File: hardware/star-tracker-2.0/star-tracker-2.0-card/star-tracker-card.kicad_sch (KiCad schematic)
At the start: 8 parts, among them J1 TFM-120-01-L-D-RA, J2 SM14B-SHLS-TF, J3 GRPB041VWVN-RC, J4 3-2492104-6

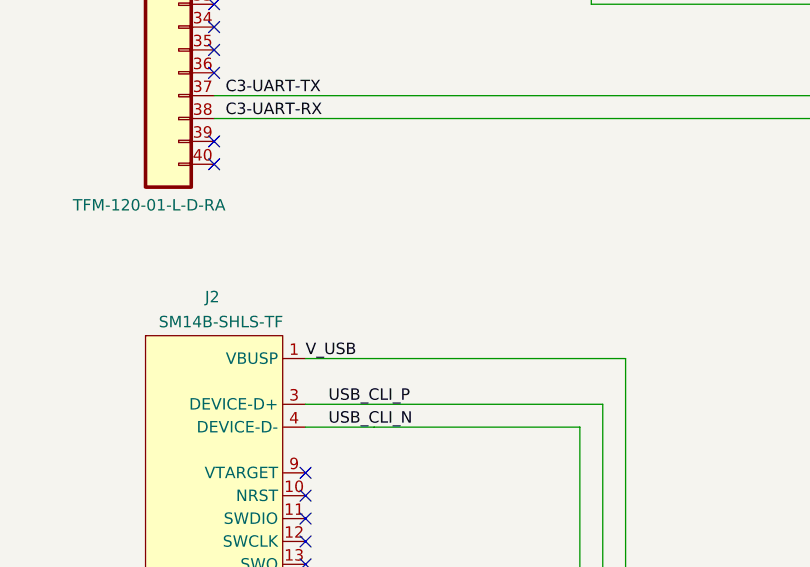
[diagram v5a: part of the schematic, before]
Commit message: Finishing touches
added gitignore for .ds_store (mac file for kicad) changed bom details for components. added 3d models to footprints. Went over schematic checklist. Camera and star tracker ready for final DR for send off.
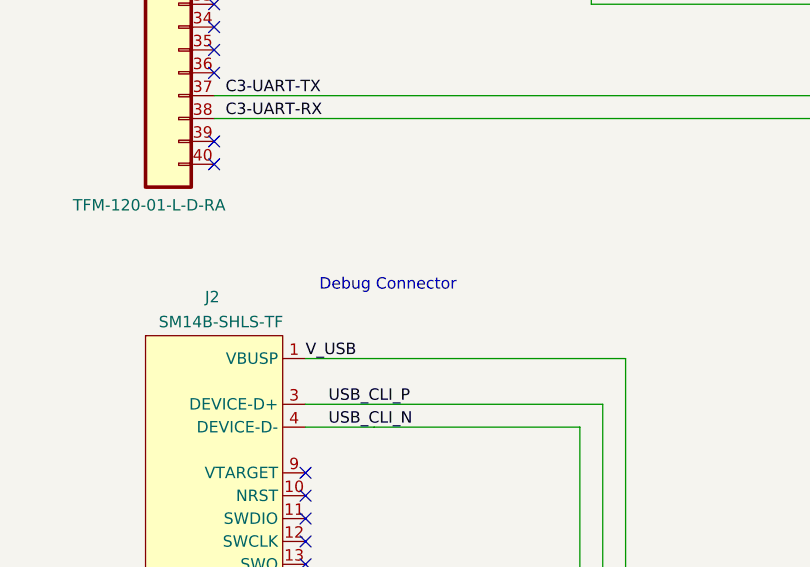
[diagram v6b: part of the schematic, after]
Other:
- note added: "Debug Connector"
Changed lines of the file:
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@@
+		)
+	)
+	(text "Debug Connector\n"
+		(exclude_from_sim no)
+		(at 58.674 138.684 0)
+		(effects
+			(font
+				(size 1.27 1.27)
+			)
+			(justify left bottom)
 		)
 	)

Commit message: Added extra Testpoints
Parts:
- added TP52: TEST-POINT, star-tracker-card:2MM-TEST-POINT, symbol star-tracker-card-eagle-import:TEST-POINT
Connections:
- net V_USB: now also TP52.1
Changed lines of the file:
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@@
 	)
 	(junction
+		(at 66.04 146.05)
+		(diameter 0)
+		(color 0 0 0 0)
+	)
+	(junction
 		(at 391.16 185.42)
 		(diameter 0)
@@
 	(wire
 		(pts
-			(xy 57.15 146.05) (xy 92.71 146.05)
+			(xy 57.15 146.05) (xy 66.04 146.05)
 		)
 		(stroke
@@
 	(wire
 		(pts
+			(xy 66.04 146.05) (xy 92.71 146.05)
+		)
+		(stroke
+			(width 0)
+			(type default)
+		)
+	)
+	(wire
+		(pts
 			(xy 179.07 185.42) (xy 179.07 81.28)
 		)
@@
 					(unit 1)
 				)
+			)
+		)
+	)
+	(symbol
+		(lib_id "star-tracker-card-eagle-import:TEST-POINT")
+		(at 66.04 146.05 180)
+		(unit 1)
+		(body_style 1)
+		(exclude_from_sim no)
+		(in_bom no)
+		(on_board yes)
+		(in_pos_files yes)
+		(dnp no)
+		(property "Reference" "TP52"
+			(at 68.58 142.24 0)
+			(show_name no)
+			(do_not_autoplace no)
+			(effects
+				(font
+					(size 1.27 1.27)
+				)
+				(justify left bottom)
+			)
+		)
+		(property "Value" "TEST-POINT"
+			(at 66.04 146.05 0)
+			(hide yes)
+			(show_name no)
+			(do_not_autoplace no)
+			(effects
+				(font
+					(size 1.27 1.27)
+				)
+			)
+		)
+		(property "Footprint" "star-tracker-card:2MM-TEST-POINT"
+			(at 66.04 146.05 0)
+			(hide yes)
+			(show_name no)
+			(do_not_autoplace no)
+			(effects
+				(font
+					(size 1.27 1.27)
+				)
+			)
+		)
+		(property "Datasheet" ""
+			(at 66.04 146.05 0)
+			(hide yes)
+			(show_name no)
+			(do_not_autoplace no)
+			(effects
+				(font
+					(size 1.27 1.27)
+				)
+			)
+		)
+		(property "Description" ""
+			(at 66.04 146.05 0)
+			(hide yes)
+			(show_name no)
+			(do_not_autoplace no)
+			(effects
+				(font
+					(size 1.27 1.27)
+				)
+			)
+		)
+		(pin "1"
+		)
+		(instances
+			(project "star-tracker-card"
+				(path "/324e9eb5-7420-4b7e-862c-cc20bb28618a"
+					(reference "TP52")
+					(unit 1)
+				)
